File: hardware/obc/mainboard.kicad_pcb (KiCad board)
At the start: 6 copper layers, 95.9 x 90.2 mm, 216 parts, among them J101 Conn_02x20_Odd_Even, J301 USB_C_Receptacle_USB2.0, J302 Conn_High-Rel_4S2P_Vertical, J303 Conn_01x06, J304 Conn_High-Rel_6P, J305 Conn_01x05, J601 Conn_01x08_Socket, J602 SMA RA Connector, J603 SMA RA Connector, J604 SMA RA Connector, Q201 BSS138DWQ-7, Q202 BSS138DWQ-7, Q203 MBT2222ADW1T1, Q204 MBT2222ADW1T1, Q205 BSS138DWQ-7, Q206 BSS138DWQ-7, Q207 MBT2222ADW1T1, Q208 MBT2222ADW1T1, Q209 MMDT2907, Q401 MBT2222ADW1T1, Q402 MBT2222ADW1T1, Q403 IRLML2803, Q404 IRF7406PbF, Q501 MMBT2222AT, Q502 IRLML2803, Q503 IRLML2803, Q504 IRLML2803, Q505 IRF7406PbF, Q506 IRF7406PbF, Q507 IRF7406PbF, U101 MAX706RESA, U102 ATSAMD51J20A-AU, U103 BMI088, U301 Mem_MT29F4G01ABAFDWB, U302 Mem_MT29F4G01ABAFDWB, U401 TPS7A4501DCQT, U402 LTC4121, U403 TPS54226PWPRPWP14_2P31X2P46-L, U404 ADM1176-1ARMZ-R7, U405 BQ25886RGER, U501 PE014006, U601 RFM98PW, U602 S1216V8, U603 GP2S1+, Y101 32.768kHz

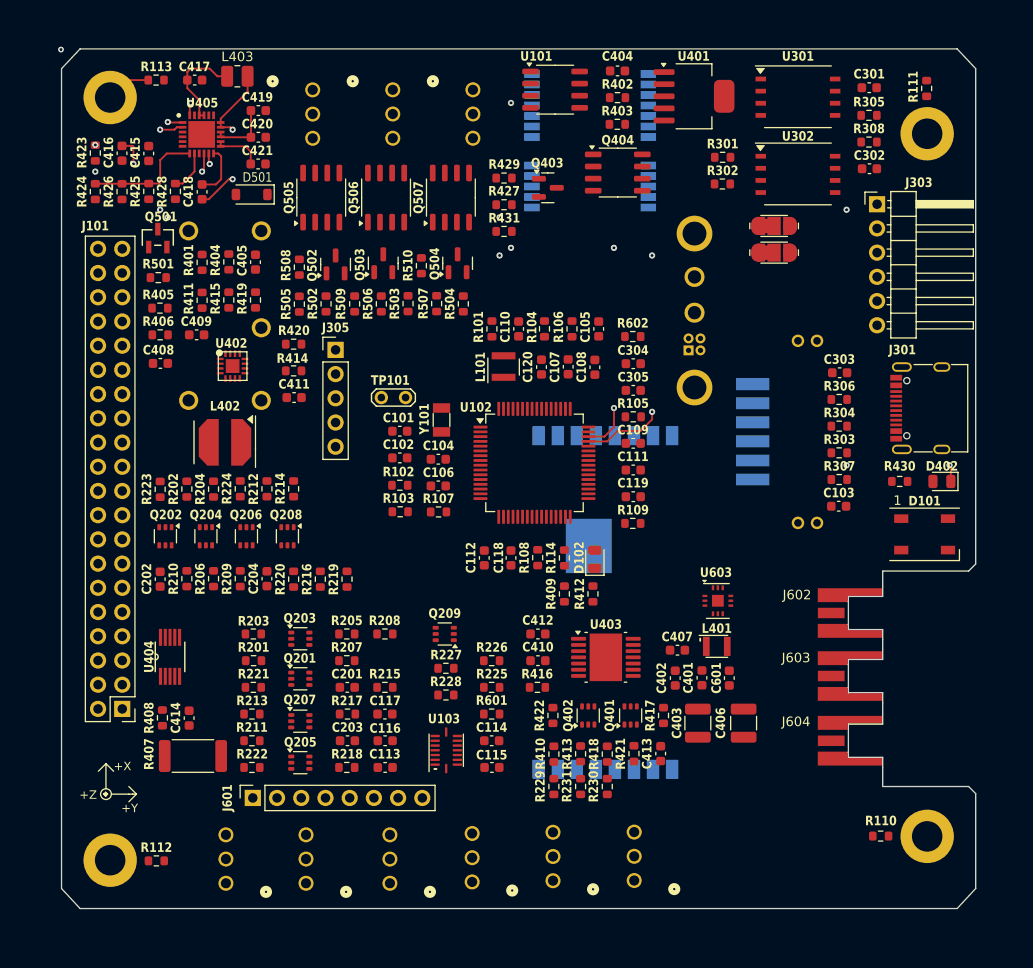
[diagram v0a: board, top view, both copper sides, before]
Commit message: obc: component reorganization
Adjusted component organization by GND & GNDREF power inputs and created planes accordingly.
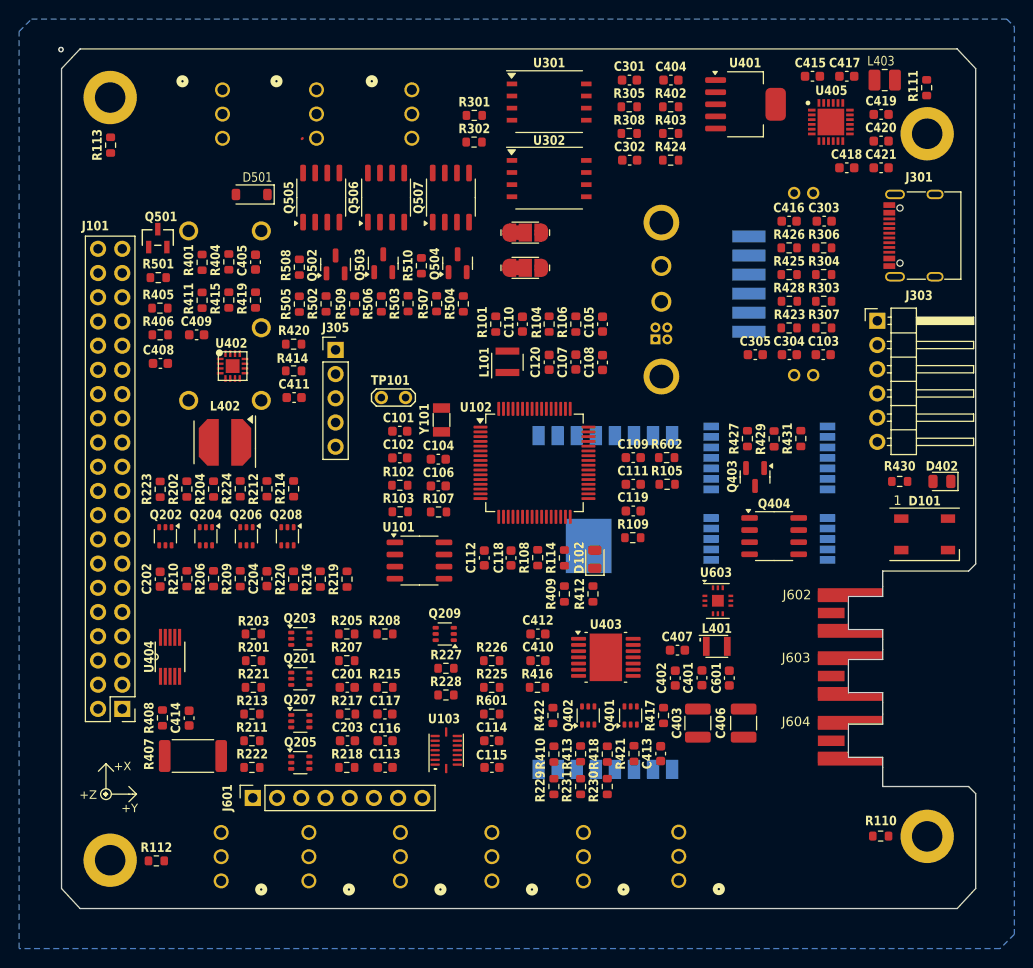
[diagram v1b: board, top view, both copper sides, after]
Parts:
- moved R423 75.1 mm to (177.2, 87.5), turned to 180 degrees
- moved C416 70.3 mm to (177.2, 76.3), turned to 180 degrees
- moved R426 70.2 mm to (177.2, 79.1), turned to 0 degrees
- moved C415 70.1 mm to (179.6, 61.1), turned to 0 degrees
- moved C417 68.4 mm to (183.2, 61.1)
- moved L403 67.9 mm to (187.2, 61.5)
- moved R425 67.7 mm to (177.2, 81.9), turned to 0 degrees
- moved C418 67.7 mm to (183.2, 70.7), turned to 180 degrees
- moved U405 66.0 mm to (181.6, 65.9)
- moved R428 65.4 mm to (177.2, 84.7), turned to 0 degrees
- moved C421 65.4 mm to (186.8, 70.7), turned to 0 degrees
- moved C419 65.3 mm to (186.8, 65.1)
- moved C420 65.3 mm to (186.8, 67.9)
- moved R424 60.4 mm to (164.8, 69.9), turned to 0 degrees
- moved U101 51.4 mm to (138.4, 111.9)
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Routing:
- net STAT: track 122.2 -> 0.00 mm, vias 5 -> 0
- net USB_D-: track 91.2 -> 0.00 mm, vias 6 -> 0
- net USB_D+: track 82.8 -> 0.00 mm, vias 5 -> 0
- net Net-(U405-SW_1): track 17.1 -> 0.00 mm, vias 2 -> 0
- net Net-(U405-ICHGSET): track 16.0 -> 0.00 mm, vias 3 -> 0
- net THM: track 12.9 -> 0.00 mm
- net /Power/REGN: track 12.6 -> 0.00 mm, vias 2 -> 0
- net Net-(U405-PMID_1): track 10.3 -> 0.00 mm
- net SYS_1&2: track 6.50 -> 0.00 mm
- net Net-(U405-BTST): track 5.55 -> 0.00 mm
- net BAT_1&2: track 5.18 -> 0.00 mm
- net Net-(H104-Pad1): track 4.99 -> 0.00 mm
- net Net-(U405-ILIM): track 4.42 -> 0.00 mm
- added copper zone on B.Cu, net GND
- added copper zone on In2.Cu, net GND
- added copper zone on In2.Cu, net GNDREF

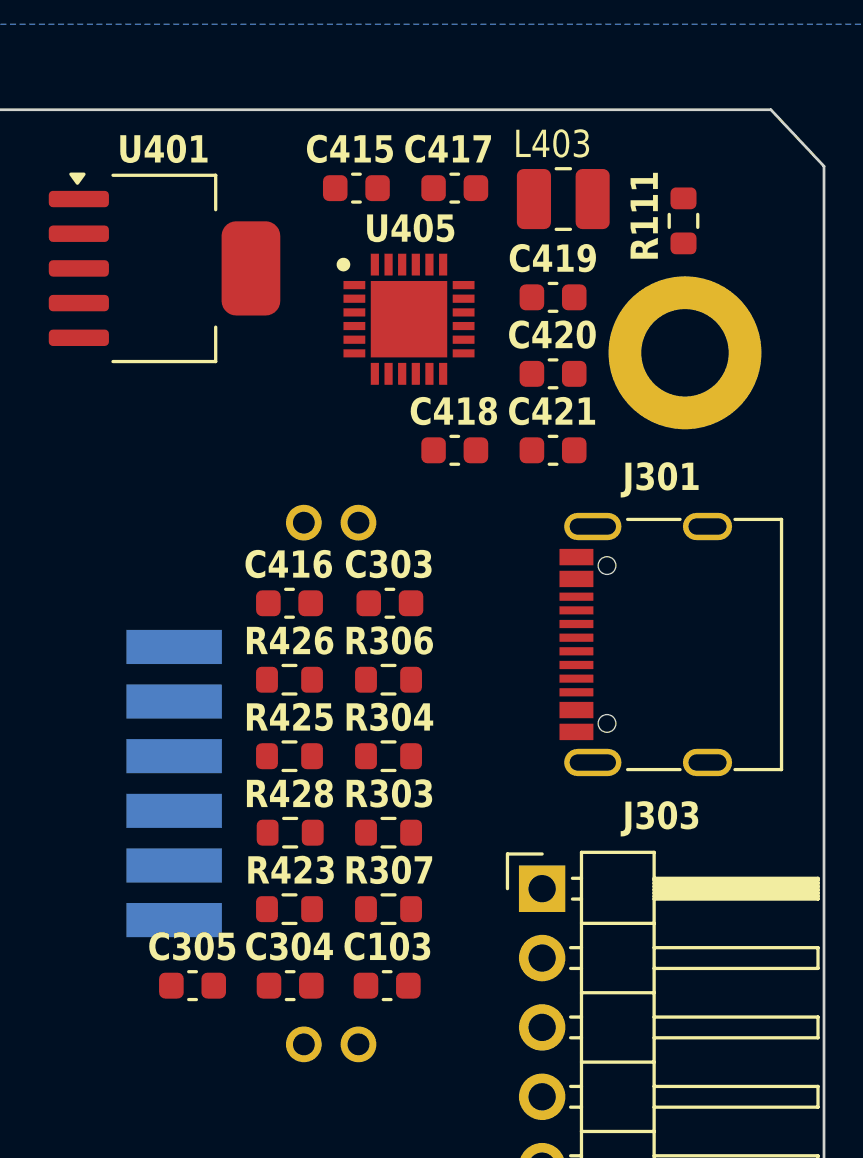
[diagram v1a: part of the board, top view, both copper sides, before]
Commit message: obc: GNDREF connections
Added vias to GNDREF plane where appropriate.
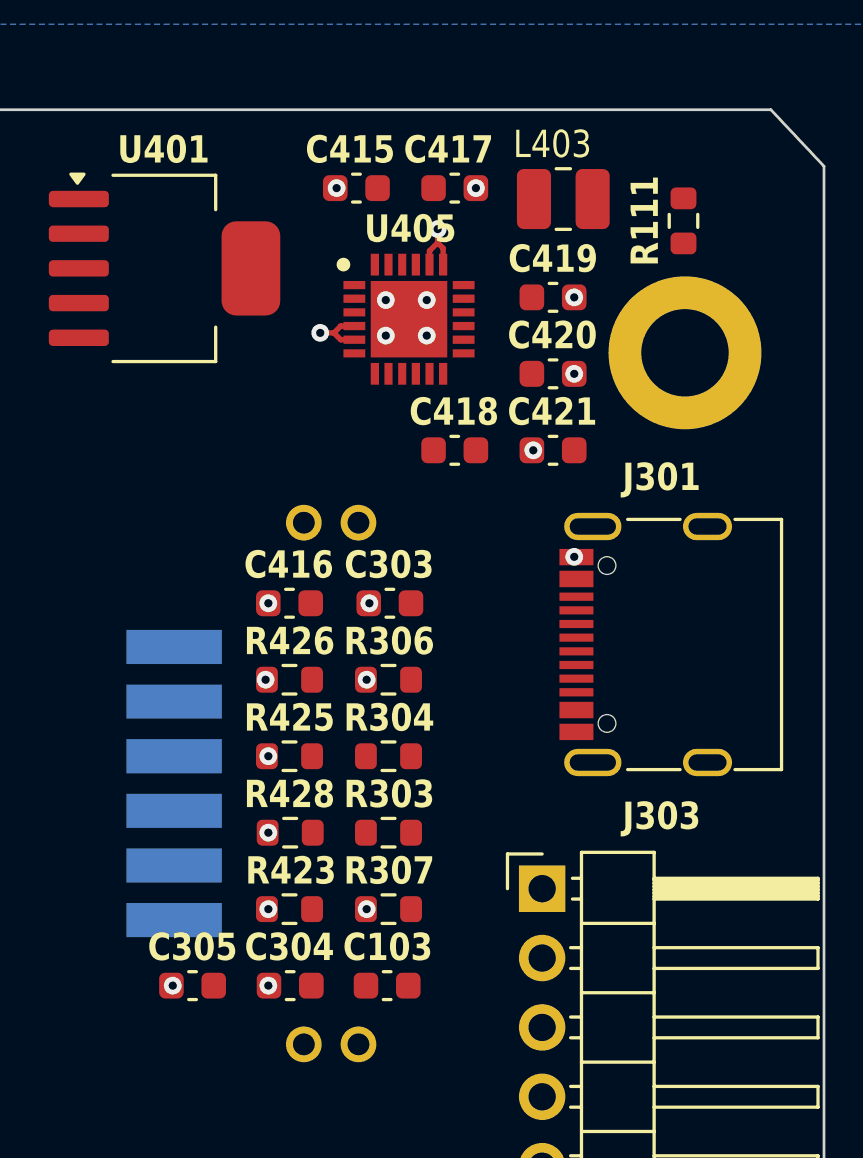
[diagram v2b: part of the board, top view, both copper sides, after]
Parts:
- turned R111 to 90 degrees
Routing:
- net GNDREF: track 0.00 -> 4.51 mm, vias 0 -> 22

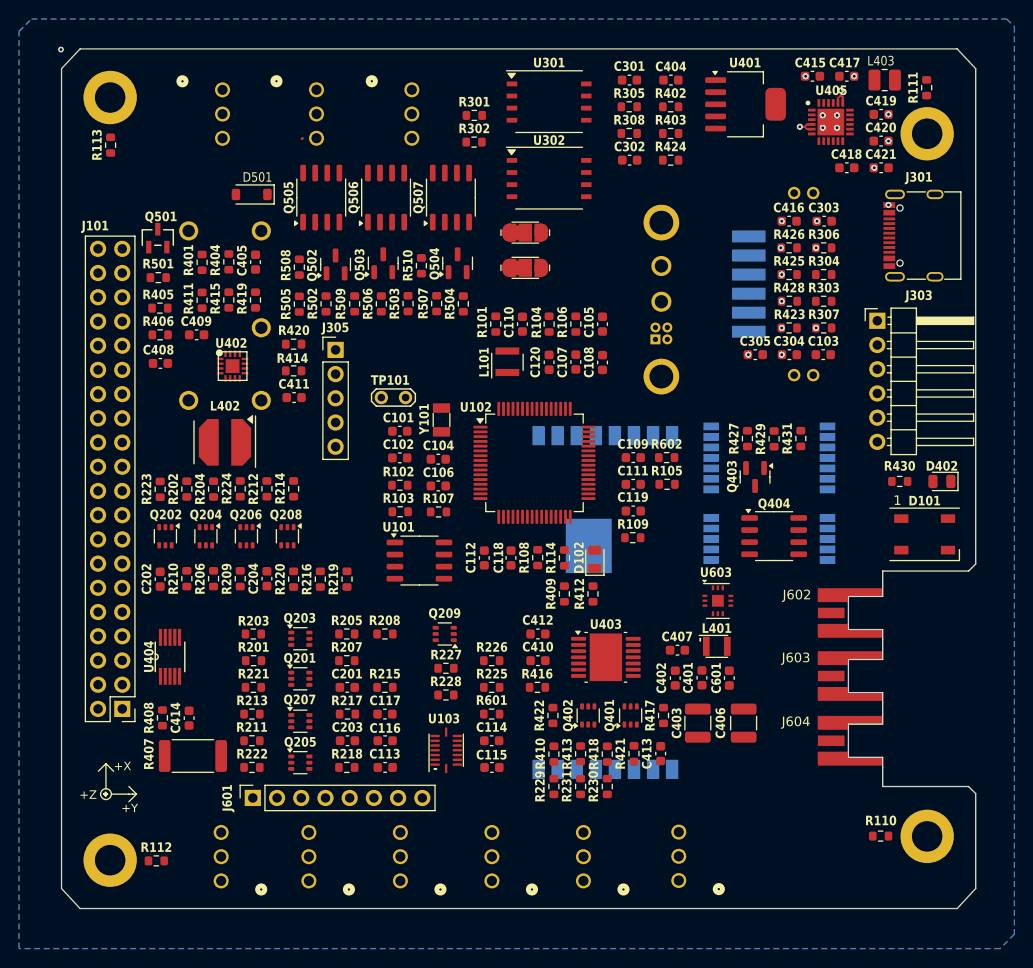
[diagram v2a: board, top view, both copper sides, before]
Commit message: obc: reorganization, power plane creation, and power connection
Adjusted placement by power input. Created power planes in layer 2 (In.1). Added ~250 vias connecting pads to power & gnd planes.
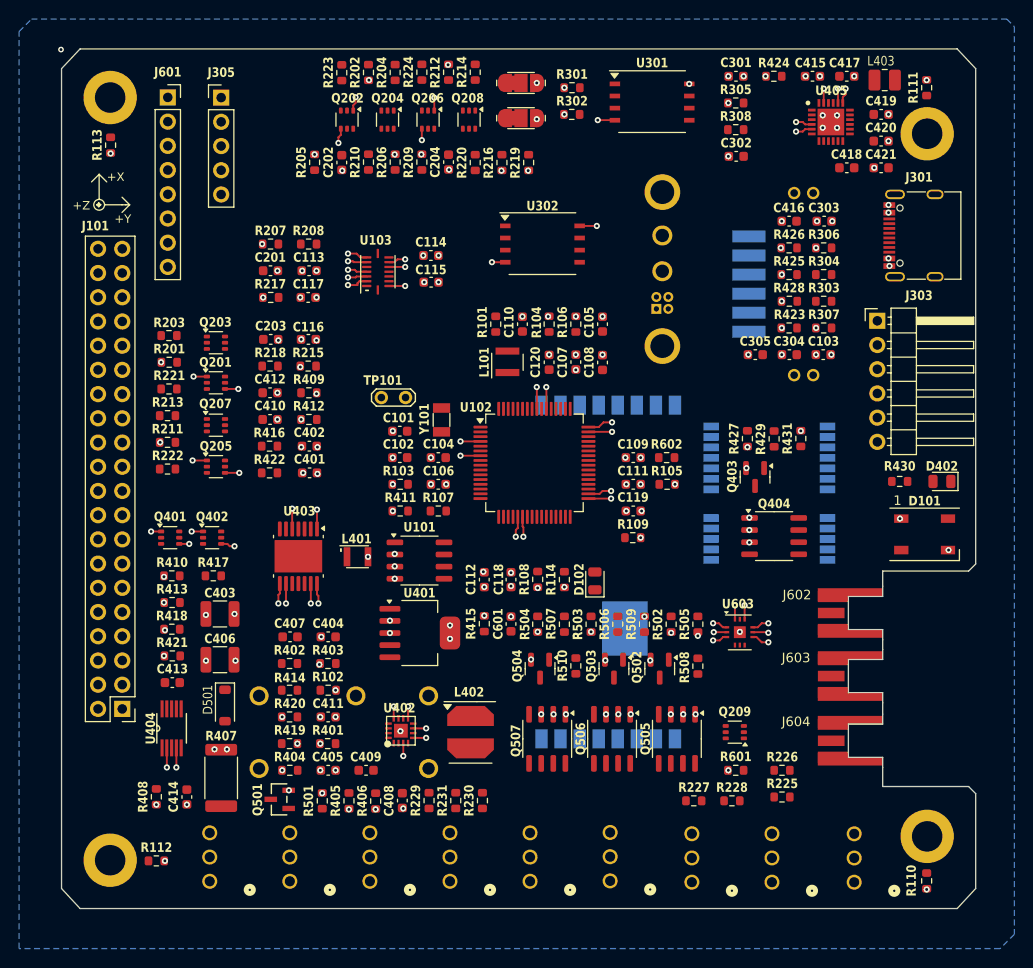
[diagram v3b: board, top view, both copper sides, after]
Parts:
- moved JP507 96.6 mm to (167.0, 145.6), turned to 90 degrees
- moved JP508 95.9 mm to (175.4, 145.6), turned to 90 degrees
- moved JP509 95.2 mm to (184.0, 145.6), turned to 90 degrees
- moved J601 74.0 mm to (112.0, 63.3), turned to 0 degrees
- moved R402 70.8 mm to (124.8, 122.7)
- moved C404 68.6 mm to (128.8, 119.9)
- moved Q505 67.9 mm to (165.4, 130.6), turned to -90 degrees
- moved R403 66.2 mm to (128.8, 122.7)
- moved U401 65.1 mm to (138.4, 119.5)
- moved Q506 61.5 mm to (158.6, 130.6), turned to -90 degrees
- moved Q501 60.3 mm to (123.7, 136.9), turned to 90 degrees
- moved R508 59.1 mm to (167.6, 123.0), turned to 90 degrees
- moved Q507 57.7 mm to (151.8, 130.6), turned to -90 degrees
- moved R501 57.5 mm to (128.2, 137.1), turned to 90 degrees
- moved R405 55.4 mm to (131.0, 137.1), turned to -90 degrees
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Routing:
- net GND: track 0.00 -> 65.9 mm, vias 0 -> 107
- net 3.3V: track 0.00 -> 21.4 mm, vias 0 -> 59
- net VBATT: track 0.00 -> 7.54 mm, vias 0 -> 17
- net GNDREF: track 4.51 -> 6.63 mm, vias 22 -> 25
- net VBUS_IN: track 0.00 -> 1.50 mm, vias 0 -> 6
- net VSOLAR: track 0.00 -> 1.35 mm, vias 0 -> 4
- net Net-(Q502-G): vias 0 -> 1
- net /Burn Wires/VBURN_A_IN: vias 0 -> 11
- added copper zone on In1.Cu, net /Burn Wires/VBURN_A_IN
- added copper zone on In1.Cu, net 3.3V
- added copper zone on In1.Cu, net VBATT
- added copper zone on In1.Cu, net VBUS_IN
- added copper zone on In1.Cu, net VSOLAR

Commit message: obc: power connection cleanup
Decreased track length to vias and centered all vias in pad. Updated schematic title blocks, edited 3D models.
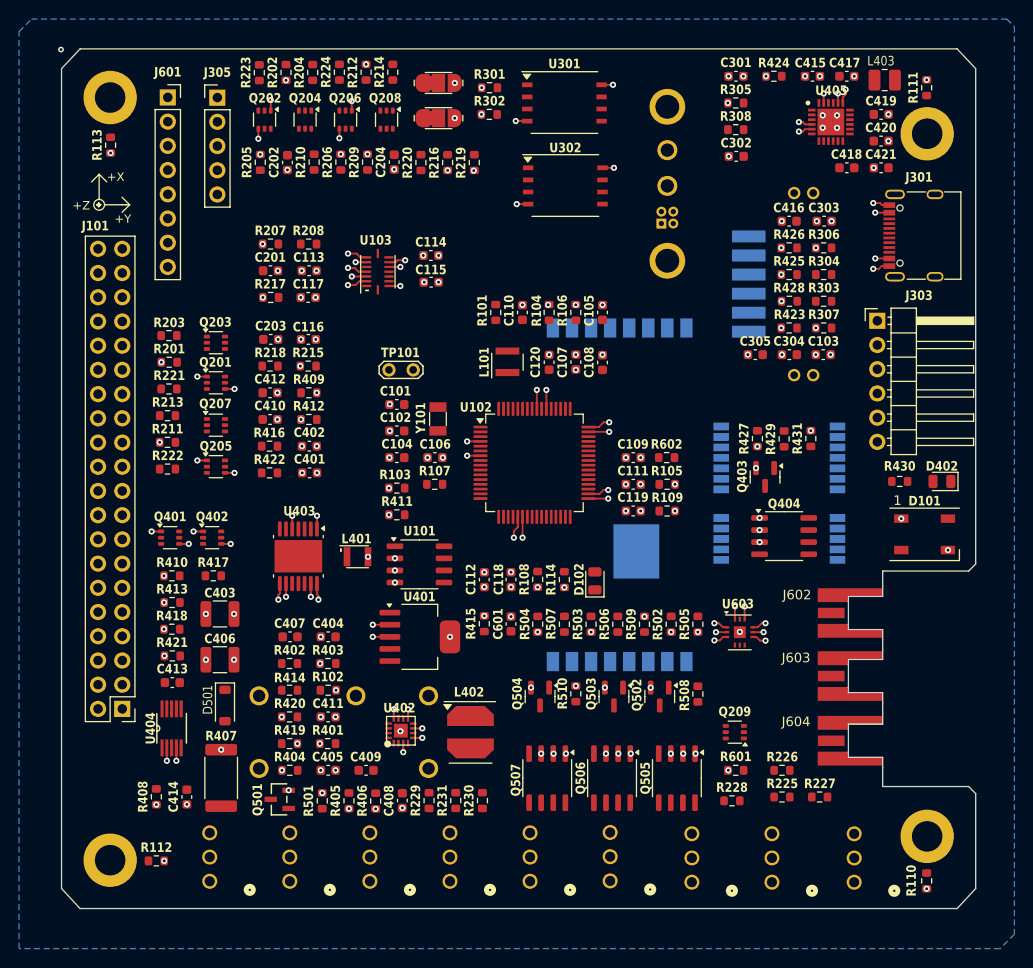
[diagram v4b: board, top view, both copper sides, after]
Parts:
- moved R227 13.2 mm to (180.4, 136.7)
- moved U301 9.20 mm to (153.6, 63.9)
- moved J302 8.97 mm to (165.2, 72.2)
- moved JP401 8.65 mm to (140.4, 61.8)
- moved JP402 8.65 mm to (140.4, 65.5)
- moved Q202 8.65 mm to (122.2, 65.7)
- moved Q204 8.65 mm to (126.4, 65.7)
- moved Q206 8.65 mm to (130.7, 65.7)
- moved Q208 8.65 mm to (134.9, 65.7)
- moved R202 8.65 mm to (124.4, 60.7)
- moved R214 8.65 mm to (135.6, 60.7)
- moved R223 8.65 mm to (121.6, 60.7)
- moved R224 8.65 mm to (130.0, 60.7)
- moved R301 8.65 mm to (145.8, 62.3)
- moved R302 8.65 mm to (145.7, 65.1)
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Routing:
- net GND: track 65.9 -> 54.1 mm, vias 107 -> 106
- net VBUS_IN: track 1.50 -> 3.95 mm
- net 3.3V: track 21.4 -> 19.1 mm
- net GNDREF: track 6.63 -> 9.00 mm
- net VBATT: track 7.54 -> 7.24 mm, vias 17 -> 16

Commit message: obc: adjusted component values
Aligned component values to proper orientation where necessary. Slight adjustments to organization and gnd plane drawing.
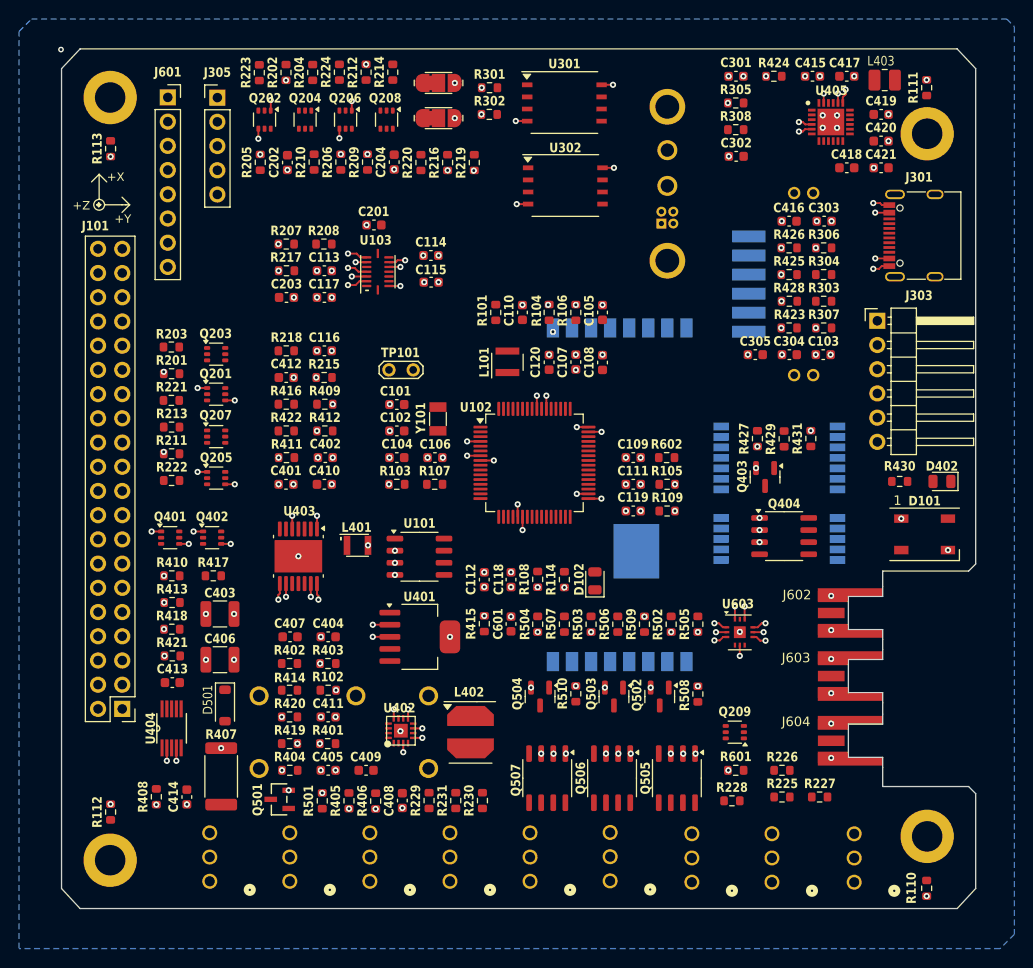
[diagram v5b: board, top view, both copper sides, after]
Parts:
- moved R411 13.0 mm to (124.5, 101.1)
- moved C201 11.9 mm to (133.6, 76.7), turned to 180 degrees
- moved C410 8.87 mm to (128.4, 103.9)
- moved R112 7.02 mm to (106.0, 138.3), turned to 90 degrees
- moved R416 4.74 mm to (124.4, 95.5)
- moved R422 4.74 mm to (124.4, 98.3)
- moved C203 4.70 mm to (124.5, 84.3)
- moved R217 3.25 mm to (124.5, 81.5)
- moved C401 2.75 mm to (124.4, 103.9)
- moved C412 2.33 mm to (124.4, 92.7)
- moved R218 2.33 mm to (124.4, 89.9)
- moved C116 2.06 mm to (128.4, 89.9)
- moved R215 2.06 mm to (128.4, 92.7)
- moved C402 2.06 mm to (128.5, 101.1)
- moved R409 2.06 mm to (128.5, 95.5)
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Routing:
- net 3.3V: track 19.1 -> 16.7 mm, vias 59 -> 61
- net GND: track 54.1 -> 52.5 mm, vias 106 -> 114
- net /Burn Wires/VBURN_A_IN: vias 11 -> 12
